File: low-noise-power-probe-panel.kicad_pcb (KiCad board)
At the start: 4 copper layers, 69.8 x 114.8 mm, 84 parts, among them J1 Amphenol 031-5431-10RFX, J2 Amphenol 031-5431-10RFX, J3 Barrel_Jack, J4 USB_C_Receptacle, J5 CONN_041X04_NO_SILK, Q1 VBI2338, SW1 SW_3PDT_x3, U1 LMP7731, U2 OPA322, U3 ADP7142AUJZ-2.5, U4 MCP73213T-A6SI/MF, U5 ADP7182AUJZ-2.5, U6 HUSB238, U7 LM334DT

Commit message: v1.0 gerbers as-manufactured
Schematic and PCB verification completed and corrections made. Add BOM,
excluding THT components, and CPL file for automated assembly.

Add script that adds 5mm edge rails to a "panel" for assembly, and add
the panel.
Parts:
- added REF**: NPTH, NPTH, F.Cu at (247.4, 22.5)
- added REF**: NPTH, NPTH, F.Cu at (172.6, 142.3)
- added REF**: Fiducial, Fiducial, F.Cu at (239.9, 22.5)
- added REF**: Fiducial, Fiducial, F.Cu at (180.1, 22.5)
- added REF**: Fiducial, Fiducial, F.Cu at (180.1, 142.3)
- added REF**: NPTH, NPTH, F.Cu at (172.6, 22.5)
- added REF**: Fiducial, Fiducial, B.Cu at (180.1, 22.5)
- added REF**: Fiducial, Fiducial, B.Cu at (180.1, 142.3)
- added REF**: Fiducial, Fiducial, B.Cu at (239.9, 22.5)
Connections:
- net +2V5 renamed Board_0-+2V5
- net -2V5 renamed Board_0--2V5
- net /+V_BAT renamed Board_0-/+V_BAT
- net /+V_BATCHG renamed Board_0-/+V_BATCHG
- net /-V_BAT renamed Board_0-/-V_BAT
- net /CHARGE_STAT renamed Board_0-/CHARGE_STAT
- net /PROBE_VGND renamed Board_0-/PROBE_VGND
- net /SCL renamed Board_0-/SCL
- net /SDA renamed Board_0-/SDA
- net /USB_CC1 renamed Board_0-/USB_CC1
- net /USB_CC2 renamed Board_0-/USB_CC2
- net /USB_D+ renamed Board_0-/USB_D+
- net /USB_D- renamed Board_0-/USB_D-
- net /USB_VBUS renamed Board_0-/USB_VBUS
- net /USB_VGND renamed Board_0-/USB_VGND
- net /V_UNREG renamed Board_0-/V_UNREG
- net Net-(BT1-Pad1) renamed Board_0-Net-(BT1-Pad1)
- net Net-(BT1-Pad2) renamed Board_0-Net-(BT1-Pad2)
- net Net-(BT2-Pad2) renamed Board_0-Net-(BT2-Pad2)
- net Net-(C1-Pad1) renamed Board_0-Net-(C1-Pad1)
- net Net-(C1-Pad2) renamed Board_0-Net-(C1-Pad2)
- net Net-(C15-Pad1) renamed Board_0-Net-(C15-Pad1)
- net Net-(C15-Pad2) renamed Board_0-Net-(C15-Pad2)
- net Net-(C2-Pad2) renamed Board_0-Net-(C2-Pad2)
- net Net-(F1-Pad1) renamed Board_0-Net-(F1-Pad1)
- net Net-(F1-Pad2) renamed Board_0-Net-(F1-Pad2)
- net Net-(F2-Pad1) renamed Board_0-Net-(F2-Pad1)
- net Net-(J5-Pad1) renamed Board_0-Net-(J5-Pad1)
- net Net-(L1-Pad1) renamed Board_0-Net-(L1-Pad1)
- net Net-(L1-Pad2) renamed Board_0-Net-(L1-Pad2)
- net Net-(Q1-Pad1) renamed Board_0-Net-(Q1-Pad1)
- net Net-(R1-Pad2) renamed Board_0-Net-(R1-Pad2)
- net Net-(R12-Pad2) renamed Board_0-Net-(R12-Pad2)
- net Net-(R13-Pad1) renamed Board_0-Net-(R13-Pad1)
- net Net-(R14-Pad1) renamed Board_0-Net-(R14-Pad1)
- net Net-(R2-Pad2) renamed Board_0-Net-(R2-Pad2)
- net Net-(R20-Pad1) renamed Board_0-Net-(R20-Pad1)
- net Net-(R20-Pad2) renamed Board_0-Net-(R20-Pad2)
- net Net-(R3-Pad1) renamed Board_0-Net-(R3-Pad1)
- net Net-(R4-Pad2) renamed Board_0-Net-(R4-Pad2)
- net Net-(R8-Pad1) renamed Board_0-Net-(R8-Pad1)
- net Net-(R9-Pad1) renamed Board_0-Net-(R9-Pad1)
- J4 pad A8: unconnected-(J4-PadA8) -> Board_0-unconnected-(J4-PadA8)
- J4 pad B8: unconnected-(J4-PadB8) -> Board_0-unconnected-(J4-PadB8)
- SW1 pad 7: unconnected-(SW1-Pad7) -> Board_0-unconnected-(SW1-Pad7)
- U4 pad 5: unconnected-(U4-Pad5) -> Board_0-unconnected-(U4-Pad5)
- U4 pad 6: unconnected-(U4-Pad6) -> Board_0-unconnected-(U4-Pad6)
- U5 pad 4: unconnected-(U5-Pad4) -> Board_0-unconnected-(U5-Pad4)
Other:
- board size 69.8 x 114.8 mm -> 79.8 x 124.8 mm
- board text added: "V-CUT"
- board text added: "low noise power probe v1.0"
- board text removed: "Stackup: 2116 * 1 impedance controlled 1.6mm total thickness HASL finish Blue soldermask"

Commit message: production files for test run
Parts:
- removed the REF** at (239.9, 22.5) (x2)
- removed the REF** at (180.1, 22.5) (x2)
- removed the REF** at (180.1, 142.3) (x2)
- added REF**: Fiducial, Fiducial, F.Cu at (180.1, 142.3)
- added REF**: Fiducial, Fiducial, F.Cu at (180.1, 22.5)
- added REF**: Fiducial, Fiducial, F.Cu at (239.9, 22.5)
- added REF**: Fiducial, Fiducial, B.Cu at (180.1, 22.5)
- added REF**: Fiducial, Fiducial, B.Cu at (239.9, 22.5)
- added REF**: Fiducial, Fiducial, B.Cu at (180.1, 142.3)
- SW1: footprint misc:Multicomp_Switch_3PDT_1M31T2B4M7QE -> misc:Switch_3PDT_C&K_7301MD9ABE
- moved RV1 1.33 mm to (183.4, 136.3)
- moved J2 0.17 mm to (216.2, 125.2)
- moved J1 0.10 mm to (197.9, 125.2)
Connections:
- net Board_0-Net-(F1-Pad2) renamed Board_0-Net-(D7-Pad2)
- net Board_0-Net-(R1-Pad2) renamed Board_0-Net-(J2-Pad1)
- net Board_0-Net-(R2-Pad2) renamed Board_0-Net-(D1-Pad2)
- net Board_0-Net-(R20-Pad1) renamed Board_0-Net-(D6-Pad2)
- net Board_0-Net-(R3-Pad1) renamed Board_0-Net-(D3-Pad2)
- net Board_0-Net-(R8-Pad1) renamed Board_0-Net-(D5-Pad1)
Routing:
- net Board_0-Net-(BT1-Pad1): track 45.1 -> 52.1 mm
- net Board_0-/+V_BAT: track 56.6 -> 51.6 mm
- net Board_0-Net-(BT1-Pad2): track 130.2 -> 126.9 mm
- net Board_0-/-V_BAT: track 35.0 -> 32.3 mm
- net Board_0-Net-(BT2-Pad2): track 25.5 -> 22.9 mm, vias 2 -> 0
- net Board_0-/+V_BATCHG: track 52.8 -> 50.8 mm
- net Board_0-/USB_VGND: track 43.4 -> 41.5 mm
- net Board_0-/PROBE_VGND: track 0.00 -> 1.38 mm, vias 163 -> 162
- net Board_0--2V5: track 78.7 -> 77.4 mm
- net Board_0-Net-(C2-Pad2): track 24.7 -> 25.2 mm
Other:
- board text added: "50Ω - 60V MAX"
- board text added: "9-16V DC 0.5A"
- board text added: "ADJUST"
- board text added: "C&K 7301MD9A"
- board text added: "FRONT PANEL"
- board text added: "OFF/CHARGE"
- board text added: "ON"
- board text added: "POWER RAIL PROBE"
- board text added: "REAR PANEL"
- board text added: "Stackup: 2116 * 1 impedance controlled 1.6mm total thickness HASL finish Blue soldermask"
- board text added: "TO REDUCE NOISE, REMOVE CABLE DURING MEASUREMENT"
- board text added: "USB-C PD 9V/12V 0.5A"
- board text added: "±25V"
- board text removed: "MULTICOMP 1M31T2B4M7QE"

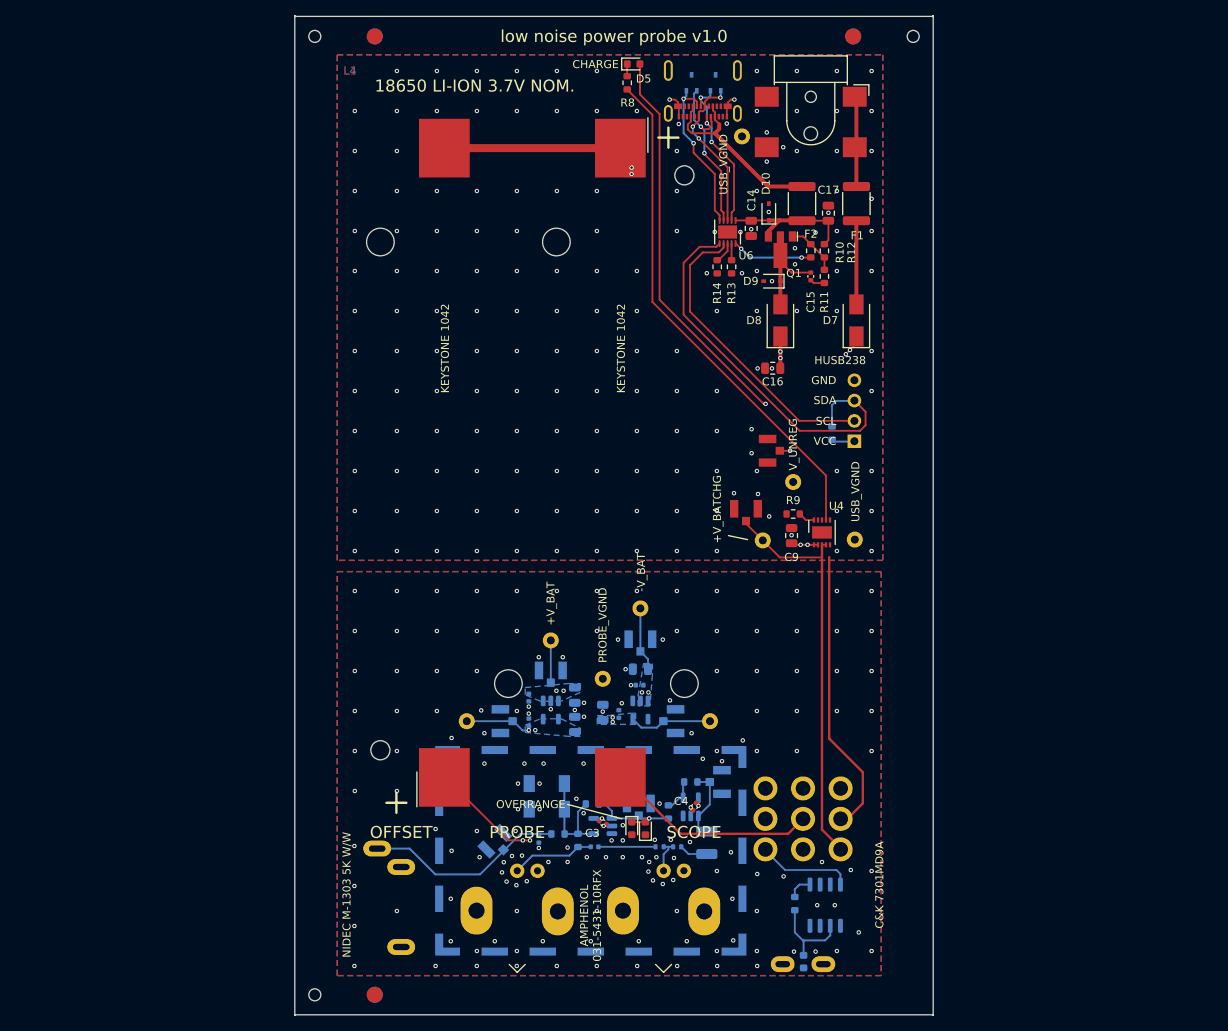
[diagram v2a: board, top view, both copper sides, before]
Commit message: v1.0.1, as manufactured
A number of small layout changes, including a switch to a dual battery
holder.

Adjust the BOM to select parts that are in stock and more commonly
available.

Mark the switch orientation clearly on silkscreen so we don't make the
same mistake again and reverse ON/CHG.
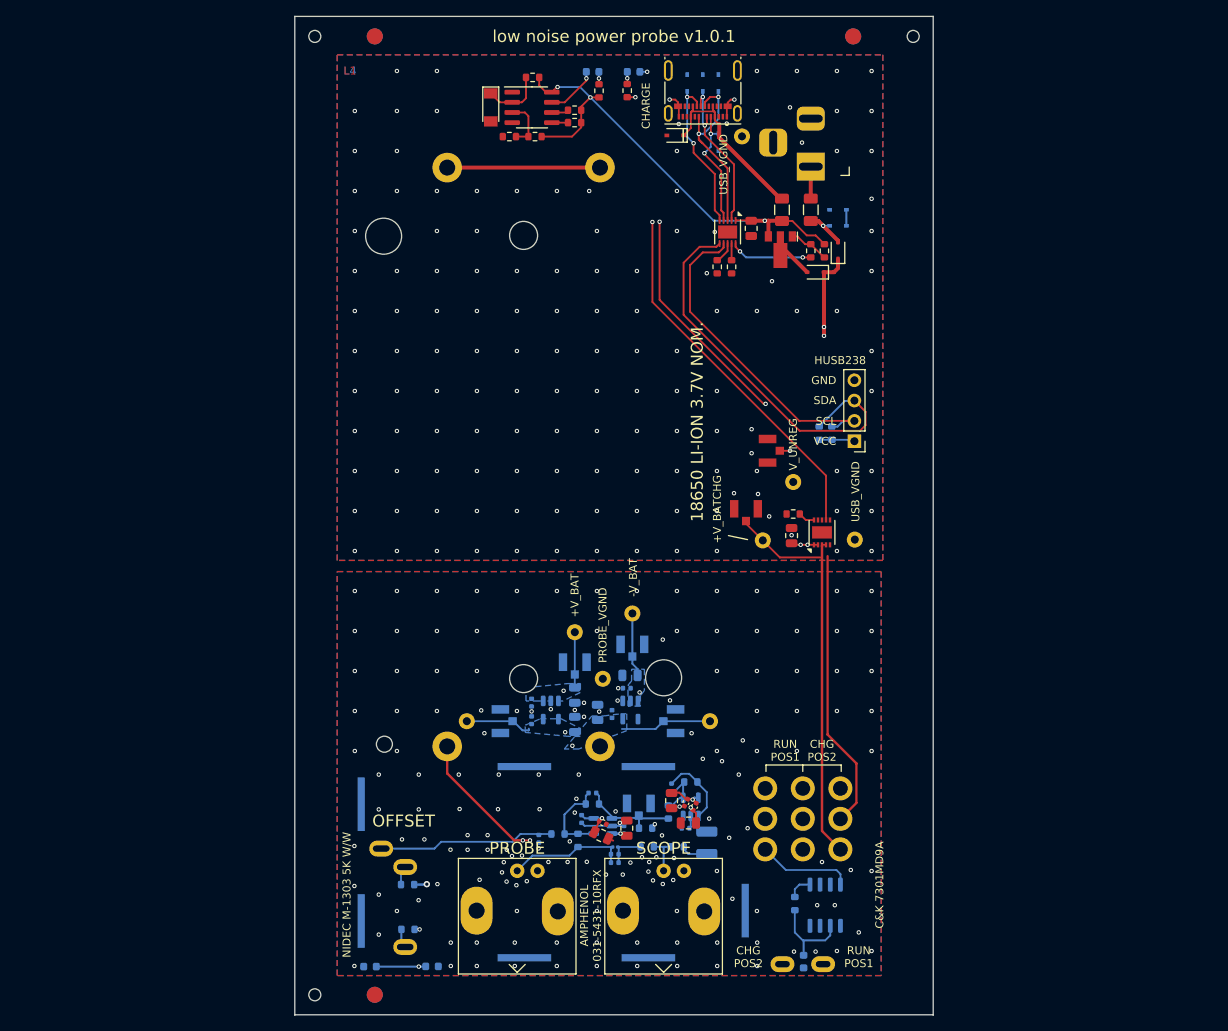
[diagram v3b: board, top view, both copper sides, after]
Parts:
- removed BT2: BATTERY-18650, Battery:BatteryHolder_Keystone_1042_1x18650
- removed C15: 100n, Capacitor_SMD:C_0402_1005Metric
- removed C16, C17: 4.7u, Capacitor_SMD:C_0805_2012Metric
- removed R11: 100R, Resistor_SMD:R_0603_1608Metric
- removed REF** (x6): Fiducial, Fiducial
- removed REF** (x3): NPTH, NPTH
- removed SHIELD1: RFShield_OnePiece, RF_Shielding:Laird_Technologies_BMI-S-205-F_38.10x25.40mm
- removed TP13: OFFSET, rf-connectors:U.FL-Hirose
- removed TP15: U2_OUT, rf-connectors:U.FL-Hirose
- added C18: DNP, Capacitor_SMD:C_0402_1005Metric, B.Cu at (210.1, 125.8)
- added C19: 27pF, Capacitor_SMD:C_0201_0603Metric, B.Cu at (210.2, 123.8)
- added C20: DNP, Capacitor_SMD:C_0402_1005Metric, B.Cu at (207.3, 117.1)
- added C21: 100n, Capacitor_SMD:C_0402_1005Metric, F.Cu at (208.6, 120.8)
- added C22: 100n, Capacitor_SMD:C_0402_1005Metric, B.Cu at (211.2, 121.7)
- added C24: 100n, Capacitor_SMD:C_0402_1005Metric, F.Cu at (219.0, 118.3)
- added C25: 100n, Capacitor_SMD:C_0402_1005Metric, B.Cu at (218.9, 121.5)
- added C26: DNP, Capacitor_SMD:C_0402_1005Metric, B.Cu at (217.2, 116.4)
- added C27: 4.7u, Capacitor_SMD:C_0805_2012Metric, F.Cu at (208.4, 122.4)
- added C28: 4.7u, Capacitor_SMD:C_0805_2012Metric, F.Cu at (211.6, 121.5)
- added C29: 4.7u, Capacitor_SMD:C_0805_2012Metric, F.Cu at (217.2, 118.0)
- added C30: 4.7u, Capacitor_SMD:C_0805_2012Metric, F.Cu at (219.3, 120.8)
- added D13: SD24-MS, misc:D_SOD-323_silkpolarity, B.Cu at (238.0, 44.2)
- added D14: SD24-MS, misc:D_SOD-323_silkpolarity, F.Cu at (217.7, 34.9)
- added D15: SD24-MS, misc:D_SOD-323_silkpolarity, B.Cu at (238.0, 46.2)
- added J10: RF Shield Clip, misc:ICSRC6508-015SFR, B.Cu at (198.8, 137.7)
- added J11: RF Shield Clip, misc:ICSRC6508-015SFR, B.Cu at (214.3, 137.7)
- added J12: RF Shield Clip, misc:ICSRC6508-015SFR, B.Cu at (226.4, 131.8)
- added J6: RF Shield Clip, misc:ICSRC6508-015SFR, B.Cu at (178.4, 118.5)
- added J7: RF Shield Clip, misc:ICSRC6508-015SFR, B.Cu at (178.4, 133.1)
- added J8: RF Shield Clip, misc:ICSRC6508-015SFR, B.Cu at (198.8, 113.8)
- added J9: RF Shield Clip, misc:ICSRC6508-015SFR, B.Cu at (214.3, 113.8)
- added KiKit_FID_B_1: Fiducial, Fiducial, B.Cu at (180.1, 22.5)
- added KiKit_FID_B_2: Fiducial, Fiducial, B.Cu at (239.9, 22.5)
- added KiKit_FID_B_3: Fiducial, Fiducial, B.Cu at (180.1, 142.3)
- added KiKit_FID_T_1: Fiducial, Fiducial, F.Cu at (180.1, 22.5)
- added KiKit_FID_T_2: Fiducial, Fiducial, F.Cu at (239.9, 22.5)
- added KiKit_FID_T_3: Fiducial, Fiducial, F.Cu at (180.1, 142.3)
- added KiKit_TO_1: NPTH, NPTH, F.Cu at (172.6, 22.5)
- added KiKit_TO_2: NPTH, NPTH, F.Cu at (247.4, 22.5)
- added KiKit_TO_3: NPTH, NPTH, F.Cu at (172.6, 142.3)
- added R16: 620, Resistor_SMD:R_0603_1608Metric, B.Cu at (184.2, 134.1)
- added R17: 620, Resistor_SMD:R_0603_1608Metric, B.Cu at (184.2, 128.5)
- added R18: DNP, Resistor_SMD:R_0603_1608Metric, F.Cu at (205.1, 33.3)
- added R19: DNP, Resistor_SMD:R_0603_1608Metric, F.Cu at (205.1, 31.7)
- added R21: 1k, Resistor_SMD:R_0603_1608Metric, F.Cu at (208.1, 29.3)
- added R22: 50k, Resistor_SMD:R_0603_1608Metric, F.Cu at (200.1, 35.0)
- added R23: 50k, Resistor_SMD:R_0603_1608Metric, F.Cu at (199.8, 27.6)
- added R24: 50k, Resistor_SMD:R_0603_1608Metric, F.Cu at (196.9, 35.0)
- added R25: 6.04k, Resistor_SMD:R_0603_1608Metric, B.Cu at (237.2, 72.1)
- added R26: 0R, Resistor_SMD:R_0603_1608Metric, B.Cu at (213.9, 121.5)
- added U8: LM311DR, Package_SO:SOIC-8_3.9x4.9mm_P1.27mm, F.Cu at (199.8, 31.4)
- BT1: value BATTERY-18650 -> Dual_Battery_Cell; footprint Battery:BatteryHolder_Keystone_1042_1x18650 -> misc:Battery-holder-18650-MYOUNG-BH-18650-A1BJ021
- C3: value 100n -> DNP; moved to B.Cu
- C4: value 100n -> DNP
- D1: value CMF04 -> Red 1.8V; footprint Diode_SMD:D_SOD-128 -> misc:LED_0603_1608Metric_polaritysilk
- D10, D9: value D22V0S1U2WS-7 -> SD24-MS; footprint Diode_SMD:D_SOD-323 -> misc:D_SOD-323_silkpolarity; moved to B.Cu
- D11, D12: value ESDA25W -> SD24-MS; footprint Package_TO_SOT_SMD:SOT-323_SC-70 -> misc:D_SOD-323_silkpolarity
- D2: value CMF04 -> 3V3; footprint Diode_SMD:D_SOD-128 -> Diode_SMD:D_MiniMELF; moved to F.Cu
- D3, D4, D5: footprint LED_SMD:LED_0603_1608Metric -> misc:LED_0603_1608Metric_polaritysilk; moved to B.Cu
- D6: footprint LED_SMD:LED_0603_1608Metric -> misc:LED_0603_1608Metric_polaritysilk
- D7, D8: value CMS04(TE12L,Q,M) -> 1N5819WS; footprint Diode_SMD:D_SMA -> Diode_SMD:D_SOD-323
- F1, F2: value MINISMDC050F-2 24V 500mA 150ms -> 30V 500mA 150ms; footprint Fuse:Fuse_1812_4532Metric -> Fuse:Fuse_1206_3216Metric
- J3: footprint misc:BarrelJack_Shou_Han_DC050-T_SMT_Horizontal -> Connector_BarrelJack:BarrelJack_Horizontal
- Q1: value VBI2338 -> WSE3099
- R1, R7: value 10R .1% 25ppm/°C -> 10R 1% 200ppm/°C; footprint Resistor_SMD:R_0402_1005Metric -> Resistor_SMD:R_0603_1608Metric
- R10: value 100k -> 50k
- R12, R15: value 22k -> 6.04k
- R8: value 1k .1% -> 1k
- R9: value 3.3k -> 5k
- U1: value LMP7731 -> OPA322
- moved D1 89.2 mm to (207.3, 26.9)
- moved D2 88.0 mm to (194.6, 31.4), turned to -90 degrees
- moved D3 38.5 mm to (179.5, 138.8), turned to 0 degrees
- moved D4 30.4 mm to (187.2, 138.8), turned to 0 degrees
- moved D10 19.1 mm to (219.2, 28.3)
- moved D9 18.6 mm to (223.1, 35.7), turned to -90 degrees
- moved BT1 9.93 mm to (198.7, 75.1)
- moved D7 9.02 mm to (238.0, 49.3)
- moved D8 7.46 mm to (235.2, 52.0), turned to 180 degrees
- moved F1 5.75 mm to (234.6, 44.2)
- moved J3 5.73 mm to (234.6, 38.8)
- moved TP3 3.17 mm to (205.1, 97.0)
- moved TP18 3.17 mm to (205.1, 100.7)
- moved C1 2.69 mm to (210.1, 124.7)
- moved C3 2.69 mm to (205.9, 120.3), turned to 90 degrees
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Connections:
- net Board_0-Net-(BT1-Pad1) renamed Board_0-Net-(BT1A-+)
- net Board_0-Net-(C1-Pad1) renamed Board_0-Net-(J1-In)
- net Board_0-Net-(D5-Pad1) renamed Board_0-Net-(D5-K)
- net Board_0-Net-(D6-Pad2) renamed Board_0-Net-(D6-A)
- net Board_0-Net-(D7-Pad2) renamed Board_0-Net-(D15-A)
- net Board_0-Net-(F2-Pad1) renamed Board_0-Net-(D14-K)
- net Board_0-Net-(J2-Pad1) renamed Board_0-Net-(J2-In)
- net Board_0-Net-(L1-Pad1) renamed Board_0-Net-(C26-Pad2)
- net Board_0-Net-(R13-Pad1) renamed Board_0-Net-(U6-ISET)
- net Board_0-Net-(R14-Pad1) renamed Board_0-Net-(U6-VSET)
- net Board_0-Net-(R4-Pad2) renamed Board_0-Net-(U2--)
- net Board_0-Net-(R9-Pad1) renamed Board_0-Net-(U4-PROG)
- net Board_0-unconnected-(J4-PadA8) renamed Board_0-unconnected-(J4-SBU1-PadA8)
- net Board_0-unconnected-(J4-PadB8) renamed Board_0-unconnected-(J4-SBU2-PadB8)
- net Board_0-unconnected-(SW1-Pad7) renamed Board_0-unconnected-(SW1C-A-Pad7)
- net Board_0-unconnected-(U4-Pad5) renamed Board_0-unconnected-(U4-NC-Pad5)
- net Board_0-unconnected-(U4-Pad6) renamed Board_0-unconnected-(U4-NC-Pad6)
- net Board_0-unconnected-(U5-Pad4) renamed Board_0-unconnected-(U5-NC-Pad4)
- BT1 pad 2: Board_0-Net-(BT1-Pad2) -> Board_0-Net-(BT1A--)
- D1 pad 1: Board_0-/PROBE_VGND -> Board_0-Net-(D1-K)
- D1 pad 2: Board_0-Net-(D1-Pad2) -> Board_0-Net-(D1-A)
- D10 pad 1: Board_0-/USB_VBUS -> Board_0-/USB_CC2
- D11 pad 2: Board_0-/USB_D+ -> Board_0-/USB_VGND
- D12 pad 1: Board_0-/USB_CC1 -> Board_0-/USB_D+
- D12 pad 2: Board_0-/USB_CC2 -> Board_0-/USB_VGND
- D2 pad 1: Board_0-Net-(D1-Pad2) -> Board_0-Net-(D2-K)
- D2 pad 2: Board_0-/PROBE_VGND -> Board_0-/USB_VGND
- D3 pad 2: Board_0-Net-(D3-Pad2) -> Board_0-Net-(D3-A)
- D4 pad 1: Board_0-Net-(D3-Pad2) -> Board_0-Net-(D3-A)
- D8 pad 2: Board_0-Net-(C15-Pad2) -> Board_0-Net-(D8-A)
- D9 pad 1: Board_0-Net-(C15-Pad2) -> Board_0-/USB_CC1
- J3 pad 3: (no net) -> Board_0-unconnected-(J3-Pad3)
- J4 pad A10: (no net) -> Board_0-unconnected-(J4-RX2--PadA10)
- J4 pad A11: (no net) -> Board_0-unconnected-(J4-RX2+-PadA11)
- J4 pad A2: (no net) -> Board_0-unconnected-(J4-TX1+-PadA2)
- J4 pad A3: (no net) -> Board_0-unconnected-(J4-TX1--PadA3)
- J4 pad B10: (no net) -> Board_0-unconnected-(J4-RX1--PadB10)
- J4 pad B11: (no net) -> Board_0-unconnected-(J4-RX1+-PadB11)
- J4 pad B2: (no net) -> Board_0-unconnected-(J4-TX2+-PadB2)
- J4 pad B3: (no net) -> Board_0-unconnected-(J4-TX2--PadB3)
- J5 pad 1: Board_0-Net-(J5-Pad1) -> Board_0-Net-(J5-Pin_1)
- Q1 pad 1: Board_0-Net-(Q1-Pad1) -> Board_0-Net-(Q1-G)
- Q1 pad 2: Board_0-Net-(C15-Pad2) -> Board_0-Net-(D8-A)
- R10 pad 1: Board_0-Net-(Q1-Pad1) -> Board_0-/USB_VBUS
- R10 pad 2: Board_0-/USB_VBUS -> Board_0-Net-(Q1-G)
- R12 pad 1: Board_0-Net-(Q1-Pad1) -> Board_0-Net-(U6-GATE)
- R12 pad 2: Board_0-Net-(R12-Pad2) -> Board_0-Net-(Q1-G)
- R15 pad 1: Board_0-Net-(J5-Pad1) -> Board_0-/SDA
- R15 pad 2: Board_0-/SDA -> Board_0-Net-(J5-Pin_1)
- R2 pad 2: Board_0-Net-(D1-Pad2) -> Board_0-Net-(U1--)
- R3 pad 1: Board_0-Net-(D3-Pad2) -> Board_0-Net-(TP14-SIGNAL)
- R3 pad 2: Board_0-Net-(D1-Pad2) -> Board_0-Net-(U1--)
- R5 pad 1: Board_0-Net-(D1-Pad2) -> Board_0-Net-(U1--)
- R6 pad 2: Board_0-Net-(D3-Pad2) -> Board_0-Net-(TP14-SIGNAL)
- RV1 pad 1: Board_0--2V5 -> Board_0-Net-(R16-Pad2)
- RV1 pad 3: Board_0-+2V5 -> Board_0-Net-(R17-Pad1)
- SW1 pad 5: Board_0-Net-(BT2-Pad2) -> Board_0-Net-(BT1B--)
- SW1 pad 8: Board_0-Net-(BT1-Pad2) -> Board_0-Net-(BT1A--)
- TP14 pad FEED: Board_0-Net-(D3-Pad2) -> Board_0-Net-(TP14-SIGNAL)
- U1 pad 1: Board_0-Net-(D3-Pad2) -> Board_0-Net-(TP14-SIGNAL)
- U1 pad 4: Board_0-Net-(D1-Pad2) -> Board_0-Net-(U1--)
- U4 pad 11: (no net) -> Board_0-unconnected-(U4-PAD-Pad11)
- U6 pad 10: Board_0-Net-(R12-Pad2) -> Board_0-Net-(U6-GATE)
- U7 pad 2: (no net) -> Board_0-unconnected-(U7-Pad2)
- U7 pad 3: (no net) -> Board_0-unconnected-(U7-Pad3)
- U7 pad 5: (no net) -> Board_0-unconnected-(U7-Pad5)
- U7 pad 7: (no net) -> Board_0-unconnected-(U7-Pad7)
- U7 pad 8: (no net) -> Board_0-unconnected-(U7-Pad8)
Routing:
- net Board_0-Net-(BT1A--): track 0.00 -> 128.0 mm
- net Board_0-Net-(BT1-Pad2): track 126.9 -> 0.00 mm, vias 2 -> 0
- net Board_0-Net-(D3-A): track 0.00 -> 51.8 mm, vias 0 -> 2
- net Board_0-/USB_VBUS: track 17.0 -> 60.8 mm, vias 0 -> 3
- net Board_0-Net-(BT1B--): track 0.00 -> 36.8 mm
- net Board_0-Net-(BT2-Pad2): track 22.9 -> 0.00 mm
- net Board_0-Net-(D1-Pad2): track 14.0 -> 0.00 mm
- net Board_0-Net-(C15-Pad2): track 11.9 -> 0.00 mm
- net Board_0-Net-(TP14-SIGNAL): track 0.00 -> 11.6 mm
- net Board_0-Net-(D3-Pad2): track 11.4 -> 0.00 mm, vias 1 -> 0
- net Board_0-Net-(U1--): track 0.00 -> 10.7 mm
- net Board_0--2V5: track 77.4 -> 88.1 mm
- net Board_0-Net-(U6-GATE): track 0.00 -> 10.4 mm, vias 0 -> 2
- net Board_0-Net-(R12-Pad2): track 10.1 -> 0.00 mm, vias 2 -> 0
- net Board_0-Net-(D2-K): track 0.00 -> 7.68 mm
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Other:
- board text added: "- >RANGE +"
- board text added: "CHG POS2"
- board text added: "MAX OFFSET: ±20V ACTIVE SIGNAL: ±1V INPUT IMPEDANCE: 50kΩ (→ 50Ω SCOPE) ATTENUATION: MAX. 1:1.2 v1.0.1 2024-06-23"
- board text added: "RUN"
- board text added: "RUN POS1"
- board text added: "low noise power probe v1.0.1"
- board text removed: "ACTIVE"
- board text removed: "KEYSTONE 1042"
- board text removed: "MAX OFFSET: ±20V ACTIVE SIGNAL: ±1V INPUT IMPEDANCE: 50kΩ (→ 50Ω SCOPE) ATTENUATION: MAX. 1:1.2 v1.0 2023-09-04"
- board text removed: "OVERRANGE"
- board text removed: "SHIELD: LAIRD BMI-S-205-F"
- board text removed: "low noise power probe v1.0"

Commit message: commit unchecked changes for 1.0.1
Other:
- board text added: "+"
- board text added: "-"
- board text added: "NIDEC M-1305 5K W/W"
- board text removed: "NIDEC M-1303 5K W/W"
